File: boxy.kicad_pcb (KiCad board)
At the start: 2 copper layers, 31.8 x 40 mm, 23 parts, among them P1 Isolated interface, Q1 Q_NPN_EBC, U1 TRIAC, U2 OPTO-TRANSISTOR, U3 OPTO-TRIAC

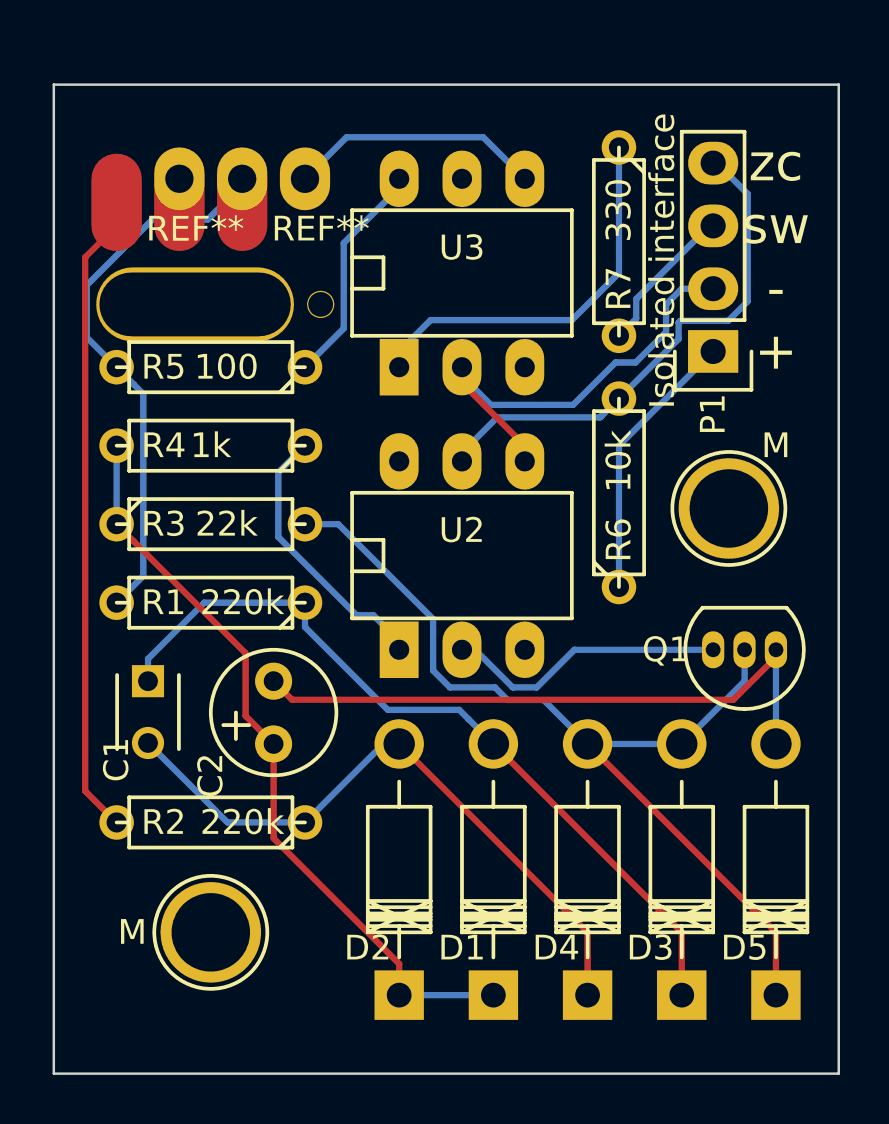
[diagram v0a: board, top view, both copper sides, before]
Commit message: revamp through hole version, add logos
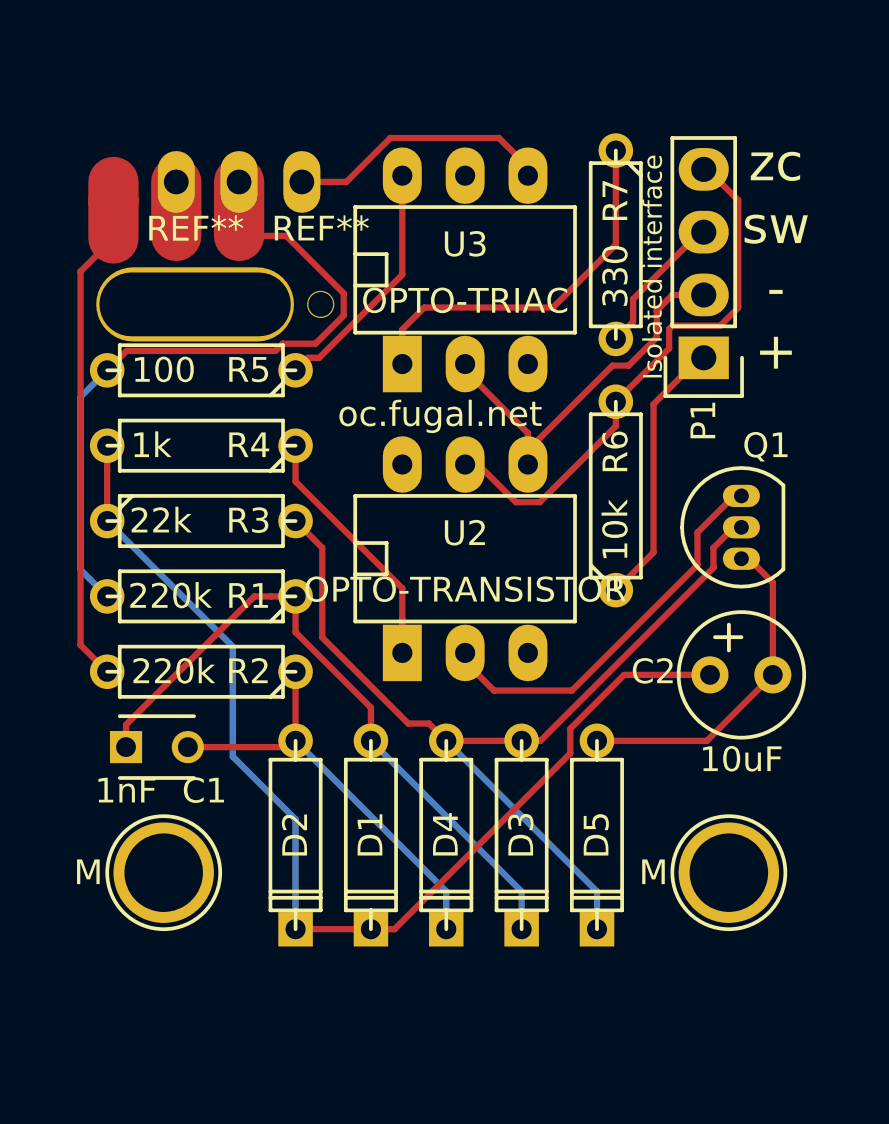
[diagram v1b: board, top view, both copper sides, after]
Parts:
- added REF**: Symbol_OSHW-Logo_SilkScreen, Symbols:Symbol_OSHW-Logo_SilkScreen, B.Cu at (42.7, 53.8)
- added REF**: OC_Logo_text, vontrapp:OC_Logo_text, B.Cu at (34.5, 38.1)
- D1, D2, D3, D4, D5: footprint Diodes_ThroughHole:Diode_DO-41_SOD81_Horizontal_RM10 -> Discret:D3
- U1: footprint Power_Integrations:TO-220 -> Transistors_TO-220:TO-220_Neutral123_Vertical
- moved C2 17.9 mm to (55.1, 47.4), turned to 0 degrees
- moved M 14.7 mm to (55.9, 55.4)
- moved D5 7.37 mm to (50.5, 53.8)
- moved D3 6.63 mm to (47.5, 53.8)
- moved R2 6.11 mm to (34.5, 47.2)
- moved D4 5.88 mm to (44.5, 53.8)
- moved D1 5.15 mm to (41.4, 53.8)
- moved D2 4.42 mm to (38.4, 53.8)
- moved Q1 3.94 mm to (56.4, 42.7), turned to 90 degrees
- moved M 3.07 mm to (33.0, 55.4)
- moved C1 2.81 mm to (31.5, 50.3), turned to 0 degrees
- moved R1 0.46 mm to (34.5, 44.2)
- moved P1 0.46 mm to (54.9, 34.5)
- moved R5 0.40 mm to (34.5, 35.1)
- moved R3 0.40 mm to (34.5, 41.1)
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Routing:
- net Net-(C2-Pad1): track 30.8 -> 44.3 mm
- net Net-(C2-Pad2): track 25.5 -> 13.6 mm
- net Net-(C1-Pad2): track 26.1 -> 17.4 mm
- net N: track 27.1 -> 20.8 mm
- net Net-(C1-Pad1): track 32.1 -> 27.2 mm
- net Net-(Q1-Pad3): track 11.4 -> 16.0 mm
- net Hot: track 24.4 -> 28.8 mm
- net Net-(P1-Pad2): track 18.8 -> 16.4 mm
- net Net-(P1-Pad4): track 21.1 -> 22.2 mm
- net Net-(R4-Pad1): track 11.1 -> 10.2 mm
- net Net-(R5-Pad1): track 9.20 -> 9.92 mm
- net Net-(R7-Pad1): track 15.9 -> 15.3 mm
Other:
- board outline removed
- board text added: "oc.fugal.net"

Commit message: add edge cuts, remove logo REF
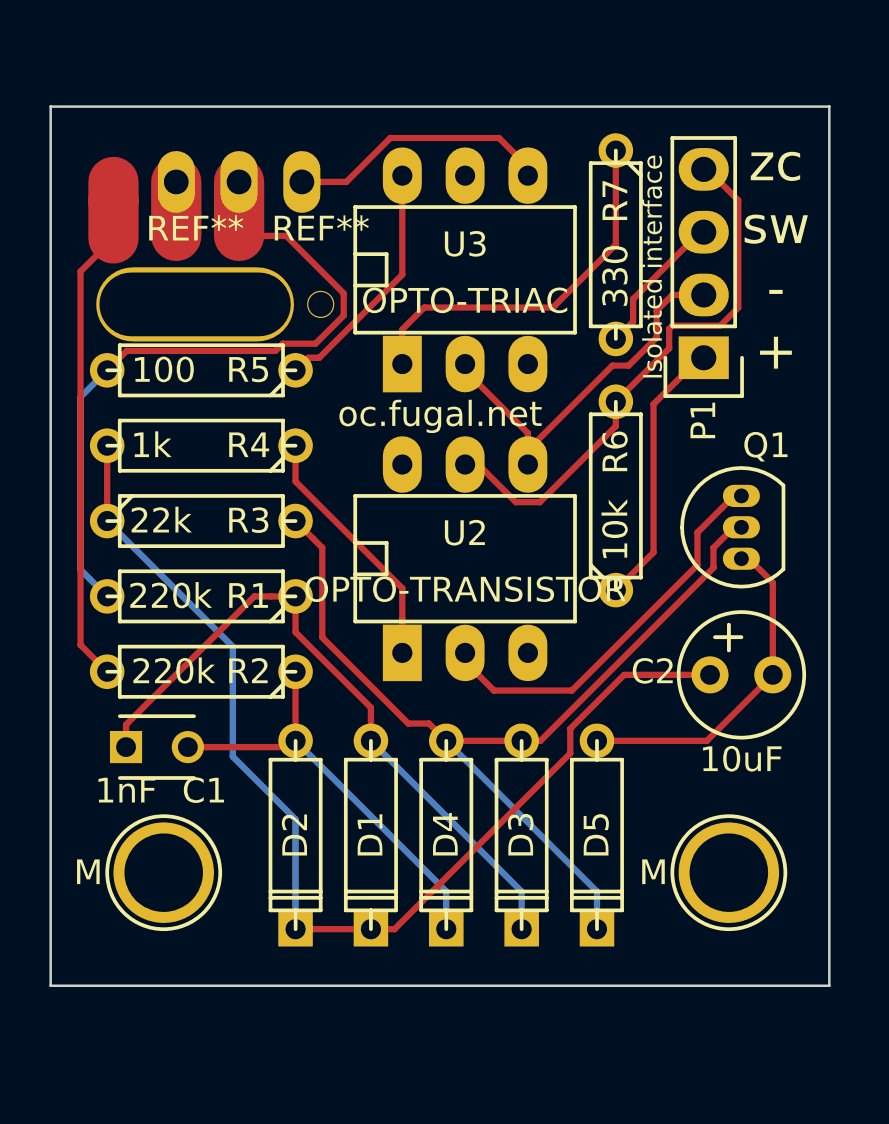
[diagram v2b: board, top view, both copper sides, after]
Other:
- board outline added: 31.5 x 35.6 mm

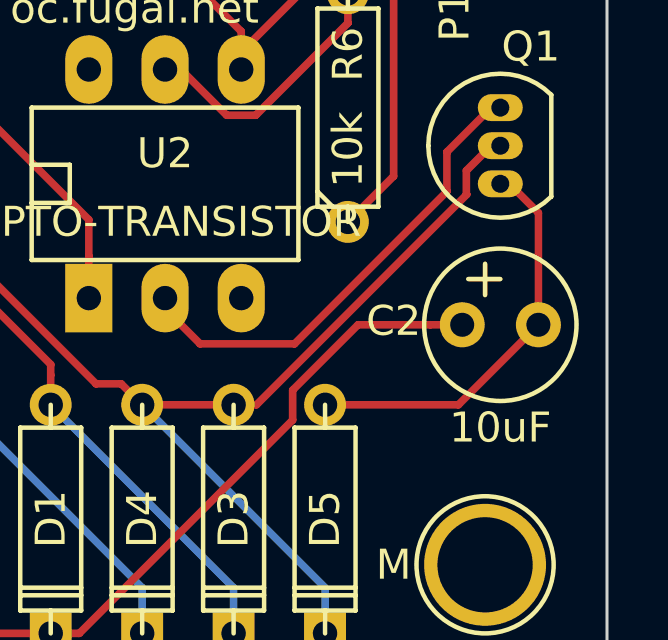
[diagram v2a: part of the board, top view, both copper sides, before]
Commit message: Change c2 footprint to one with 3d
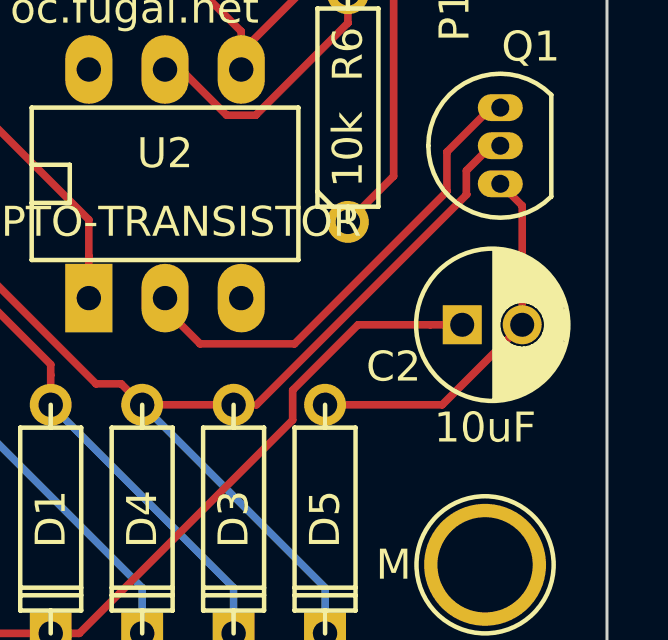
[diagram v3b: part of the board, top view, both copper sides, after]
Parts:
- C2: footprint Capacitors_Elko_ThroughHole:Elko_vert_11x5mm_RM2.5 -> Capacitors_ThroughHole:C_Radial_D5_L11_P2
- Q1: value Q_NPN_EBC -> NPN
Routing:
- net Net-(C2-Pad2): track 13.6 -> 13.0 mm

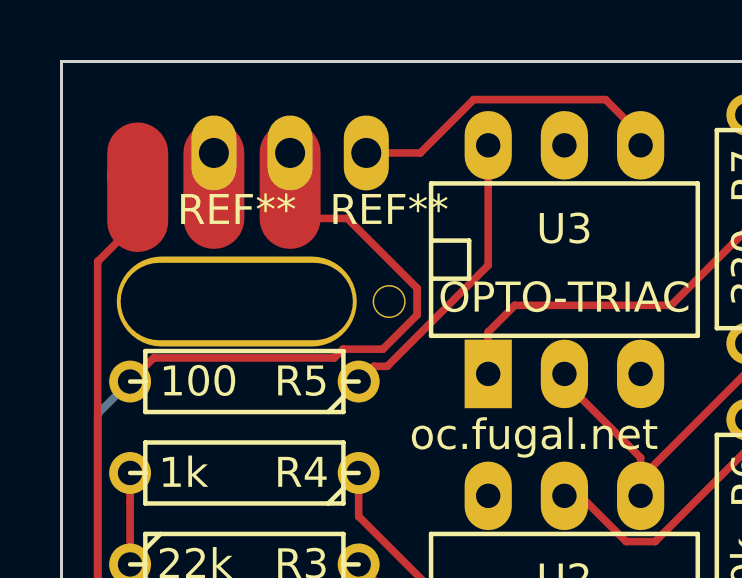
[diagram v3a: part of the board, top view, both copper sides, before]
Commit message: use edge-cut for wire slot
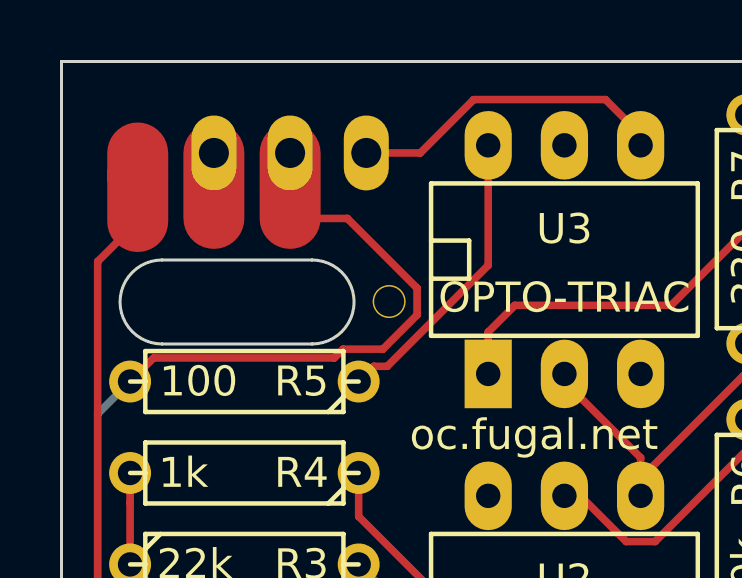
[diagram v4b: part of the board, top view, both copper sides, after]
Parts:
- removed the REF** at (34.3, 32.4)
- REF**: value 1pin -> (none)
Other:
- outline, holes or cut-outs redrawn
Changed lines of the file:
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@@
     (links 29)
     (no_connects 0)
-    (area 28.397999 24.333999 59.994001 59.994001)
+    (area 25.706618 22.443 61.395155 59.994001)
     (thickness 1.6)
-    (drawings 12)
+    (drawings 16)
     (tracks 125)
     (zones 0)
-    (modules 25)
+    (modules 24)
     (nets 19)
   )
@@
       (drillshape 0)
       (scaleselection 1)
-      (outputdirectory /run/media/vontrapp/KIRK/boxy/))
+      (outputdirectory /home/vontrapp/Dropbox/code/tronics/pics/))
   )
   (net 0 "")
@@
   )
   (module Connect:1pin (layer F.Cu)
-    (at 34.29 32.385)
-    (descr "module 1 pin (ou trou mecanique de percage)")
-    (tags DEV)
-    (fp_text reference REF** (at 0 -3.048) (layer F.SilkS)
-      (effects (font (size 1 1) (thickness 0.15)))
-    )
-    (fp_text value 1pin (at -1.778 0) (layer F.Fab)
-      (effects (font (size 1 1) (thickness 0.15)))
-    )
-    (pad "" thru_hole oval (at 0 0) (size 8 3) (drill oval 7.74 2.58) (layers *.Cu *.Mask F.SilkS))
-  )
-  (module Connect:1pin (layer F.Cu)
     (at 39.37 32.385)
     (descr "module 1 pin (ou trou mecanique de percage)")
     (tags DEV)
-    (fp_text reference REF** (at 0 -3.048) (layer F.SilkS)
-      (effects (font (size 1 1) (thickness 0.15)))
-    )
-    (fp_text value 1pin (at -2.413 0) (layer F.Fab)
+    (fp_text reference REF** (at 0 -3.048) (layer F.SilkS) hide
+      (effects (font (size 1 1) (thickness 0.15)))
+    )
+    (fp_text value "" (at -2.413 0) (layer F.Fab) hide
       (effects (font (size 1 1) (thickness 0.15)))
     )
@@
     )
   )
+  (gr_line (start 36.8 33.8) (end 31.8 33.8) (angle 90) (layer Edge.Cuts) (width 0.1))
+  (gr_line (start 31.8 31) (end 36.8 31) (angle 90) (layer Edge.Cuts) (width 0.1))
+  (gr_arc (start 36.8 32.4) (end 36.8 31) (angle 180) (layer Edge.Cuts) (width 0.1))
+  (gr_arc (start 31.8 32.4) (end 31.8 33.8) (angle 180) (layer Edge.Cuts) (width 0.1))
   (gr_line (start 59.944 24.384) (end 28.448 24.384) (angle 90) (layer Edge.Cuts) (width 0.1))
   (gr_line (start 59.944 59.944) (end 59.944 24.384) (angle 90) (layer Edge.Cuts) (width 0.1))
@@
   (segment (start 39.160383 33.972499) (end 40.301001 32.831881) (width 0.254) (layer F.Cu) (net 2))
   (segment (start 30.988 28.194) (end 30.988 27.432) (width 2.032) (layer F.Cu) (net 3))
+  (segment (start 29.654499 31.051501) (end 30.988 29.718) (width 0.254) (layer F.Cu) (net 3))
+  (segment (start 29.654499 46.164499) (end 29.654499 31.051501) (width 0.254) (layer F.Cu) (net 3))
+  (segment (start 30.734 47.244) (end 29.654499 46.164499) (width 0.254) (layer F.Cu) (net 3))
   (segment (start 30.988 29.718) (end 30.988 28.194) (width 2.032) (layer F.Cu) (net 3))
-  (segment (start 30.734 47.244) (end 29.654499 46.164499) (width 0.254) (layer F.Cu) (net 3))
-  (segment (start 29.654499 46.164499) (end 29.654499 31.051501) (width 0.254) (layer F.Cu) (net 3))
-  (segment (start 29.654499 31.051501) (end 30.988 29.718) (width 0.254) (layer F.Cu) (net 3))
   (segment (start 47.498 57.658) (end 47.498 56.134) (width 0.254) (layer B.Cu) (net 4))
   (segment (start 47.498 56.134) (end 41.402 50.038) (width 0.254) (layer B.Cu) (net 4))
